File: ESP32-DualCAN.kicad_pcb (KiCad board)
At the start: 2 copper layers, 19.6 x 44.5 mm, 47 parts, among them J1 USB_C_Receptacle_USB2.0_14P, J2 705510040, J3 holes, J4 holes, J5 pads, SW1 Reset, SW2 Boot, U1 LV2862Y, U2 ESP32-C6-MINI-1, U3 SN65HVD230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

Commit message: Moved CAN0 pins.  Added UART tap points.
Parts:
- added ?: , clipboard:fc211d7d-06df-4809-892a-d774031bd53d, B.Cu at (135.1, 74.3)
- added J6: Aux1, Connector_PinHeader_1.00mm:PinHeader_1x06_P1.00mm_Horizontal, B.Cu at (136.8, 86.3)
- added REF**: OSHW-Logo2_7.3x6mm_SilkScreen, Symbol:OSHW-Logo2_7.3x6mm_SilkScreen, B.Cu at (130.6, 91.9)
- SW1: value Reset -> Rst
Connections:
- U2 pad 26: unconnected-(U2-IO20-Pad26) -> CAN0_TXD
- U2 pad 27: unconnected-(U2-IO21-Pad27) -> CAN0_RXD
- U2 pad 28: unconnected-(U2-IO22-Pad28) -> UART1_RX
- U2 pad 29: unconnected-(U2-IO23-Pad29) -> UART1_TX
- U2 pad 30: CAN0_RXD -> UART0_RX
- U2 pad 31: CAN0_TXD -> UART0_TX
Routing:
- net +3.3V: track 50.8 -> 60.8 mm, vias 6 -> 7
- net CAN0_TXD: track 13.5 -> 9.52 mm
- net Net-(U2-IO9): track 22.8 -> 24.9 mm
- net UART0_TX: track 0.00 -> 1.64 mm
- net UART0_RX: track 0.00 -> 1.56 mm
- net CAN0_RXD: track 14.6 -> 13.1 mm
- net UART1_TX: track 0.00 -> 1.48 mm
- net UART1_RX: track 0.00 -> 1.40 mm
- net GND: vias 53 -> 52
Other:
- board text added: "${REVISION}"

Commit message: silk
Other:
- board text added: "3.3 G TX0 RX0 TX1 RX1"
- board text added: "Vin G 1L 1H 0H 0L"
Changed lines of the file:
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@@
 		(layer "Edge.Cuts")
+	)
+	(gr_text "Vin G  1L  1H  0H 0L"
+		(at 139.05 117.8 0)
+		(layer "B.SilkS")
+		(effects
+			(font
+				(size 1 1.15)
+				(thickness 0.15)
+			)
+			(justify left bottom mirror)
+		)
+	)
+	(gr_text "3.3\nG\nTX0\nRX0\nTX1\nRX1"
+		(at 136.3 86.6 0)
+		(layer "B.SilkS")
+		(effects
+			(font
+				(size 0.6 0.4)
+				(thickness 0.1)
+			)
+			(justify left bottom mirror)
+		)
 	)
 	(gr_text "${REVISION}"

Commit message: ESP32-C6-Zero main
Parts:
- removed ?: , clipboard:fc211d7d-06df-4809-892a-d774031bd53d
- removed C4, C6: 100n, Capacitor_SMD:C_0402_1005Metric
- removed D1: ESDA5V3L, Package_DFN_QFN:Diodes_DFN1006-3
- removed D2: DSK38, Diode_SMD:D_SOD-123F
- removed D5: Yellow, LED_SMD:LED_0603_1608Metric
- removed D7, D8: H5VNT2B, Package_TO_SOT_SMD:SOT-23
- removed the J1 at (122.1, 99.7)
- removed the J6 at (136.8, 86.3)
- removed R1, R2: 5.11K, Resistor_SMD:R_0402_1005Metric
- removed R10, R11, R7: 470, Resistor_SMD:R_0402_1005Metric
- removed R12, R13: 120Ω, Resistor_SMD:R_1206_3216Metric_Pad1.30x1.75mm_HandSolder
- removed R14, R15: 22, Resistor_SMD:R_0402_1005Metric
- removed R4: 51k, Resistor_SMD:R_0402_1005Metric
- removed R5, R6: 10k, Resistor_SMD:R_0402_1005Metric
- removed REF**: OSHW-Logo2_7.3x6mm_SilkScreen, Symbol:OSHW-Logo2_7.3x6mm_SilkScreen
- removed SW1: Rst, Button_Switch_SMD:SW_SPST_TS-1088-xR020
- removed SW2: Boot, Button_Switch_SMD:SW_SPST_TS-1088-xR020
- added J2: Conn_01x10_Socket, Connector_PinSocket_2.54mm:PinSocket_1x10_P2.54mm_Vertical, F.Cu at (136.9, 80.8)
- added J3: Conn_01x10_Socket, Connector_PinSocket_2.54mm:PinSocket_1x10_P2.54mm_Vertical, F.Cu at (121.7, 80.8)
- added J7: pads, Connector_Wire:SolderWire-0.1sqmm_1x06_P3.6mm_D0.4mm_OD1mm, B.Cu at (138.3, 115.2)
- J1: renamed from J2; value 705510040 -> Molex 70553 6p; footprint lib:CONN_70551-xxxx_06_MOL -> lib:CONN_705530005_06_MOL
- R8: value 51k -> 68k
- R9: value 15k -> 12k
- U2: value ESP32-C6-MINI-1 -> ESP32-C6-Zero; footprint RF_Module:ESP32-C6-MINI-1 -> Waveshare-ESP32:Waveshare-ESP32-C6-Zero; moved to B.Cu
- U3, U4: value SN65HVD230 -> TCAN1044AV
- moved R9 13.2 mm to (124.8, 81.5), turned to -90 degrees
- moved C7 13.1 mm to (129.3, 80.3), turned to 0 degrees
- moved L1 11.8 mm to (132.0, 81.5), turned to 0 degrees
- moved U1 11.6 mm to (126.8, 81.8), turned to -90 degrees
- moved R8 11.2 mm to (124.8, 83.2), turned to -90 degrees
- moved C5 11.1 mm to (134.6, 83.8), turned to -90 degrees
- moved D6 9.41 mm to (129.3, 82.9), turned to -90 degrees
- moved C8 8.69 mm to (131.3, 83.5), turned to 180 degrees
- moved C3 7.84 mm to (127.1, 84.6), turned to 0 degrees
- moved C9 7.34 mm to (131.2, 84.5), turned to 180 degrees
- moved U2 6.55 mm to (129.8, 90.8), turned to 180 degrees
- moved D3 6.46 mm to (129.8, 101.2)
- moved C1 5.76 mm to (126.6, 86.8), turned to 0 degrees
- moved U4 5.62 mm to (130.8, 96.8), turned to 180 degrees
- moved C13 4.81 mm to (134.8, 96.7), turned to -90 degrees
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- renumbered J3 to J4, J4 to J6
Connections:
- C12 pad 1: +3.3V -> +5V
- C13 pad 1: +3.3V -> +5V
- C5 pad 1: +3.3V -> +5V
- C8 pad 1: +3.3V -> +5V
- C9 pad 1: +3.3V -> +5V
- L1 pad 2: +3.3V -> +5V
- R8 pad 2: +3.3V -> +5V
- U2 pad 1: GND -> +5V
- U2 pad 10: unconnected-(U2-IO5-Pad10) -> Net-(J3-Pin_9)
- U2 pad 11: GND -> Net-(J3-Pin_8)
- U2 pad 12: CAN0_RS -> Net-(J3-Pin_7)
- U2 pad 14: GND -> CAN0_RS
- U2 pad 15: unconnected-(U2-IO6-Pad15) -> Net-(J3-Pin_4)
- U2 pad 16: unconnected-(U2-IO7-Pad16) -> Net-(J3-Pin_3)
- U2 pad 4: unconnected-(U2-NC-Pad4) -> CAN0_RXD
- U2 pad 5: Net-(U2-IO2) -> CAN0_TXD
- U2 pad 6: unconnected-(U2-IO3-Pad6) -> CAN1_RXD
- U2 pad 7: unconnected-(U2-NC-Pad7) -> CAN1_TXD
- U2 pad 9: unconnected-(U2-IO4-Pad9) -> Net-(J2-Pin_9)
- U3 pad 3: +3.3V -> +5V
- U3 pad 4: Net-(U3-R) -> CAN0_RXD
- U3 pad 5: unconnected-(U3-Vref-Pad5) -> +3.3V
- U4 pad 3: +3.3V -> +5V
- U4 pad 4: Net-(U4-R) -> CAN1_RXD
- U4 pad 5: unconnected-(U4-Vref-Pad5) -> +3.3V
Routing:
- net +3.3V: track 60.8 -> 17.0 mm, vias 7 -> 0
- net +5V: track 0.00 -> 42.3 mm, vias 0 -> 2
- net Net-(U2-IO9): track 24.9 -> 0.00 mm, vias 2 -> 0
- net USB_D-: track 21.6 -> 0.00 mm, vias 2 -> 0
- net USB_D+: track 21.2 -> 0.00 mm, vias 3 -> 0
- net GND: track 38.3 -> 52.0 mm, vias 52 -> 47
- net CAN0_L: track 22.8 -> 35.0 mm
- net Net-(D2-A): track 11.5 -> 0.00 mm
- net CAN0_H: track 21.3 -> 31.9 mm
- net +BATT: track 10.7 -> 20.4 mm
- net CAN0_RXD: track 13.1 -> 3.97 mm, vias 2 -> 0
- net CAN1_RS: track 18.7 -> 9.67 mm, vias 2 -> 1
- net /BATT_Diode: track 19.8 -> 27.7 mm
- net CAN0_RS: track 14.4 -> 7.65 mm, vias 2 -> 1
- net Net-(J2-Pin_8): track 6.80 -> 0.00 mm
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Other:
- board size 19.6 x 44.5 mm -> 19.6 x 38.8 mm
- board text added: "5V 3V G"
- board text added: "G 3V 5V"
- board text added: "RX TX"
- board text added: "TX RX"
- board text added: "Works with ESP32-C6-Zero in the back or ESP32-C6-SuperMini on the front terminals"
- board text removed: "3.3 G TX0 RX0 TX1 RX1"

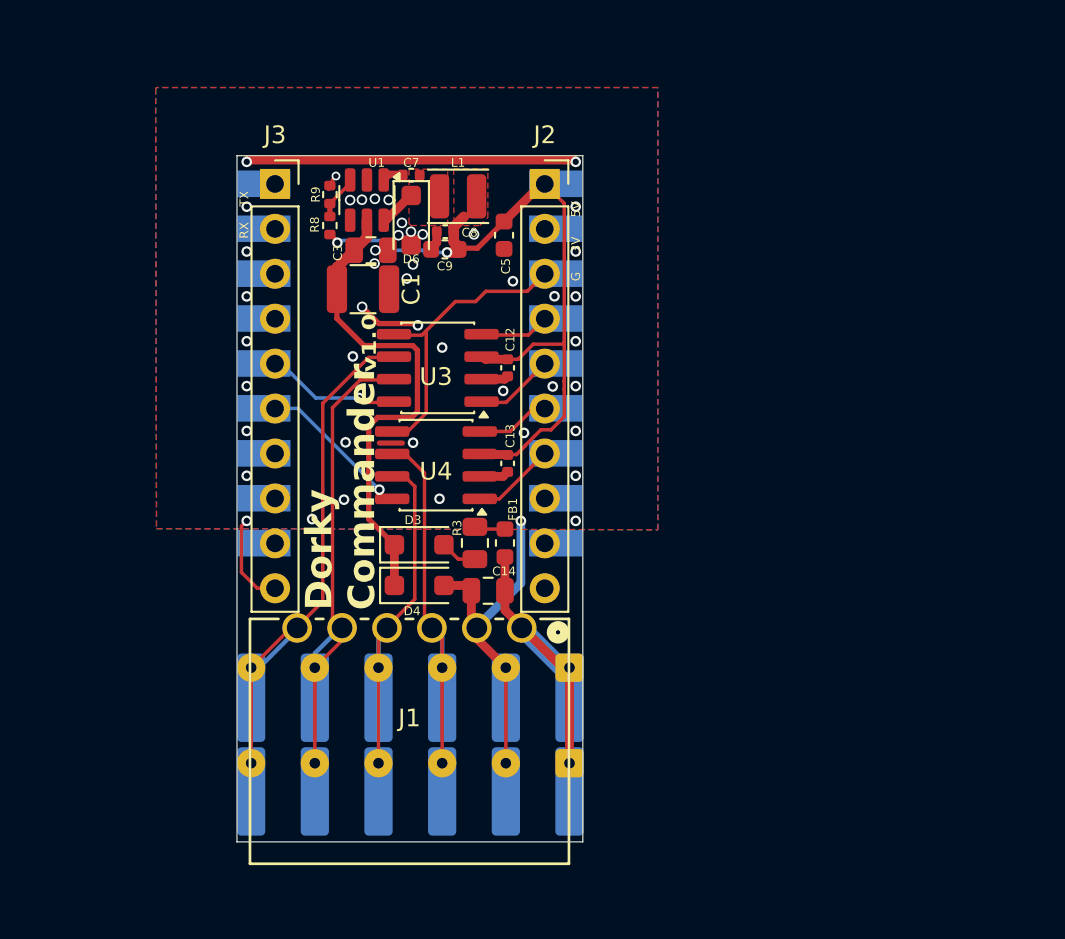
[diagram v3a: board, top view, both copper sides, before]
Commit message: ESP32-C6-SuperMini as main
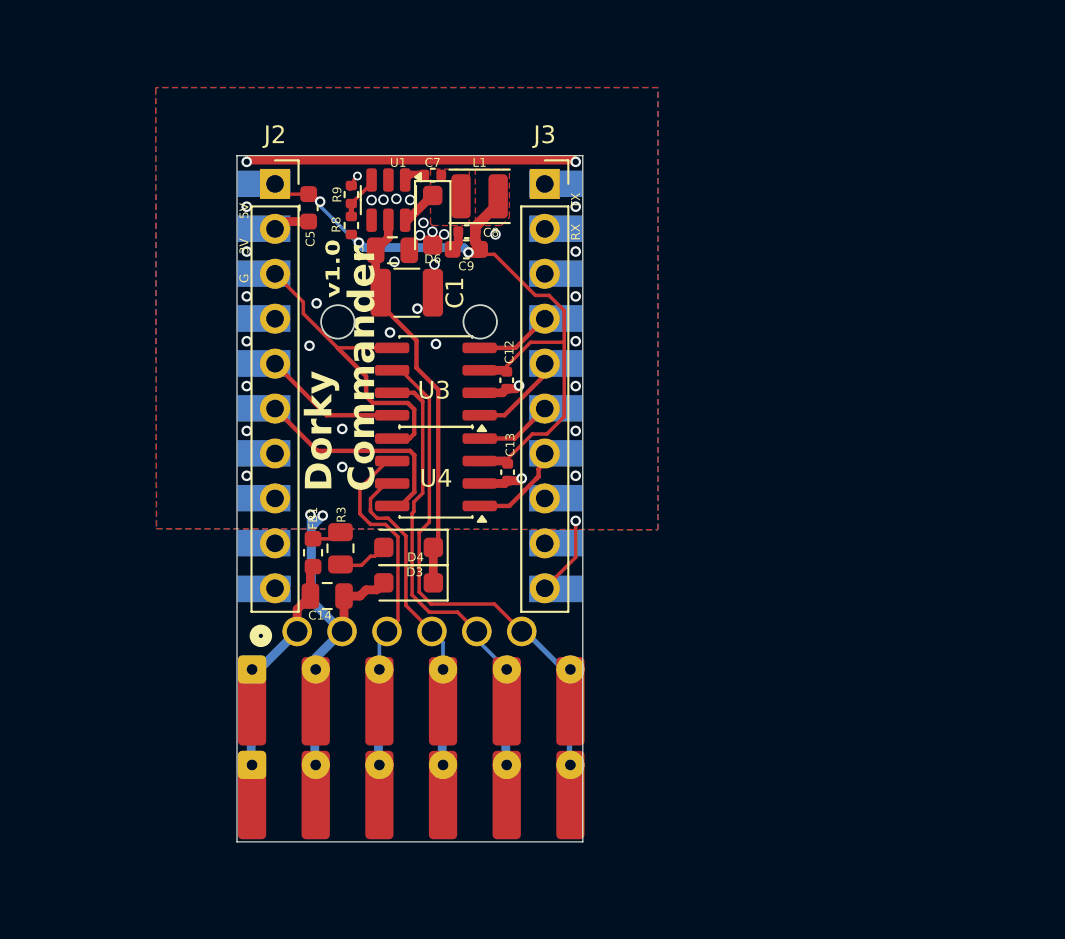
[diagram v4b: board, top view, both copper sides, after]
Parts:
- J1: moved to B.Cu
- J4, J5, J6, J7: moved to F.Cu
- U2: value ESP32-C6-Zero -> ESP32-C6-SuperMini; footprint Waveshare-ESP32:Waveshare-ESP32-C6-Zero -> lib:ESP32-C6-SuperMini
- moved J5 18.0 mm to (120.3, 110.1), turned to 0 degrees
- moved J7 18.0 mm to (120.3, 115.4), turned to 0 degrees
- moved J4 18.0 mm to (120.3, 113.7), turned to 0 degrees
- moved J6 17.9 mm to (120.4, 108.3), turned to 0 degrees
- moved J1 12.7 mm to (122.9, 106.2), turned to 180 degrees
- moved C5 11.2 mm to (123.5, 82.2)
- moved FB1 10.9 mm to (123.8, 101.7)
- moved C14 9.10 mm to (124.6, 104.2), turned to 0 degrees
- moved R3 7.61 mm to (125.3, 101.5)
- moved C1 2.48 mm to (129.1, 87.0)
- moved C7 1.22 mm to (130.6, 80.3)
- moved C8 1.22 mm to (132.5, 83.5)
- moved C9 1.22 mm to (132.5, 84.5)
- moved D6 1.22 mm to (130.6, 82.9)
- moved L1 1.22 mm to (133.2, 81.5)
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- renumbered J3 to J2, J2 to J3
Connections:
- J2 pad 1: Net-(J3-Pin_1) -> +5V
- J2 pad 10: GND -> Net-(J2-Pin_10)
- J2 pad 2: Net-(J3-Pin_2) -> GND
- J2 pad 3: Net-(J3-Pin_3) -> +3.3V
- J2 pad 4: Net-(J3-Pin_4) -> Net-(J2-Pin_4)
- J2 pad 7: Net-(J3-Pin_7) -> Net-(J2-Pin_7)
- J2 pad 8: Net-(J3-Pin_8) -> Net-(J2-Pin_8)
- J2 pad 9: Net-(J3-Pin_9) -> Net-(J2-Pin_9)
- J3 pad 1: +5V -> Net-(J3-Pin_1)
- J3 pad 10: unconnected-(J2-Pin_10-Pad10) -> GND
- J3 pad 2: GND -> Net-(J3-Pin_2)
- J3 pad 3: +3.3V -> Net-(J3-Pin_3)
- J3 pad 8: Net-(J2-Pin_8) -> Net-(J3-Pin_8)
- J3 pad 9: Net-(J2-Pin_9) -> Net-(J3-Pin_9)
- U2 pad 10: Net-(J3-Pin_9) -> Net-(J2-Pin_10)
- U2 pad 11: Net-(J3-Pin_8) -> GND
- U2 pad 12: Net-(J3-Pin_7) -> Net-(J3-Pin_9)
- U2 pad 13: CAN1_RS -> Net-(J3-Pin_8)
- U2 pad 14: CAN0_RS -> CAN1_TXD
- U2 pad 15: Net-(J3-Pin_4) -> CAN1_RXD
- U2 pad 16: Net-(J3-Pin_3) -> CAN0_TXD
- U2 pad 17: Net-(J3-Pin_2) -> CAN0_RXD
- U2 pad 18: Net-(J3-Pin_1) -> Net-(J3-Pin_3)
- U2 pad 4: CAN0_RXD -> Net-(J2-Pin_4)
- U2 pad 5: CAN0_TXD -> CAN0_RS
- U2 pad 6: CAN1_RXD -> CAN1_RS
- U2 pad 7: CAN1_TXD -> Net-(J2-Pin_7)
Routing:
- net +BATT: track 20.4 -> 13.1 mm
- net CAN0_H: track 31.9 -> 25.6 mm
- net CAN0_L: track 35.0 -> 29.6 mm
- net CAN1_H: track 24.1 -> 18.9 mm
- net CAN1_L: track 25.2 -> 20.0 mm
- net /BATT_Diode: track 27.7 -> 22.7 mm
- net CAN1_RS: track 9.67 -> 12.6 mm, vias 1 -> 0
- net (no net): track 1.30 -> 0.00 mm
- net GND: track 52.0 -> 53.1 mm, vias 47 -> 40
- net +3.3V: track 17.0 -> 17.9 mm
- net Net-(D3-A): track 2.09 -> 2.89 mm
- net +5V: track 42.3 -> 43.1 mm, vias 2 -> 3
- net CAN0_TXD: track 4.50 -> 5.26 mm
- net CAN1_TXD: track 4.74 -> 5.47 mm
- net CAN0_RS: track 7.65 -> 7.83 mm, vias 1 -> 0
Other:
- outline, holes or cut-outs redrawn
- board text added: "ESP32-C6-SuperMini"
- board text removed: "Works with ESP32-C6-Zero in the back or ESP32-C6-SuperMini on the front terminals"

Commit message: cleanup
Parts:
- moved C1 0.35 mm to (129.4, 87.0)
- moved C3 0.06 mm to (128.3, 84.6)

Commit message: horizontal layout
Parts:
- moved J2 37.3 mm to (158.8, 83.0), turned to -90 degrees
- moved C5 34.1 mm to (157.5, 84.9), turned to 180 degrees
- moved J7 34.0 mm to (124.3, 81.6), turned to -90 degrees
- moved R9 32.8 mm to (158.2, 87.3), turned to 180 degrees
- moved J4 32.6 mm to (126.0, 81.6), turned to -90 degrees
- moved C7 31.0 mm to (159.3, 91.9), turned to -90 degrees
- moved U1 30.8 mm to (157.9, 89.4), turned to 180 degrees
- moved R8 30.8 mm to (156.5, 87.3), turned to 180 degrees
- moved J5 30.0 mm to (129.6, 81.6), turned to -90 degrees
- moved J6 28.9 mm to (131.4, 81.6), turned to -90 degrees
- moved L1 28.1 mm to (158.2, 94.6), turned to -90 degrees
- moved J3 28.0 mm to (158.8, 98.2), turned to -90 degrees
- moved D6 27.7 mm to (156.8, 91.9), turned to 180 degrees
- moved C3 27.2 mm to (155.1, 89.7), turned to -90 degrees
- moved C8 25.8 mm to (156.2, 93.8), turned to 90 degrees
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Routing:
- net GND: track 53.1 -> 63.1 mm, vias 40 -> 41
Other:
- board size 19.6 x 38.8 mm -> 38.8 x 19.6 mm
